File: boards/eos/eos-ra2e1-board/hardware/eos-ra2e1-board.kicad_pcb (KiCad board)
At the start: 2 copper layers, 68.6 x 53.3 mm, 62 parts, among them J1 USB-C, J2 SWD, J3 D8-SCL, J4 D0-D7, J5 POWER, J6 A0-A5, J7 PMOD A, J8 PMOD B, SW1 RESET, SW2 USER, U1 R7FA2E1A92DFM, U2 SP0503BAHTG, U3 CP2102N-A02-GQFN24, U4 TPS7A91, Y1 32.768kHz

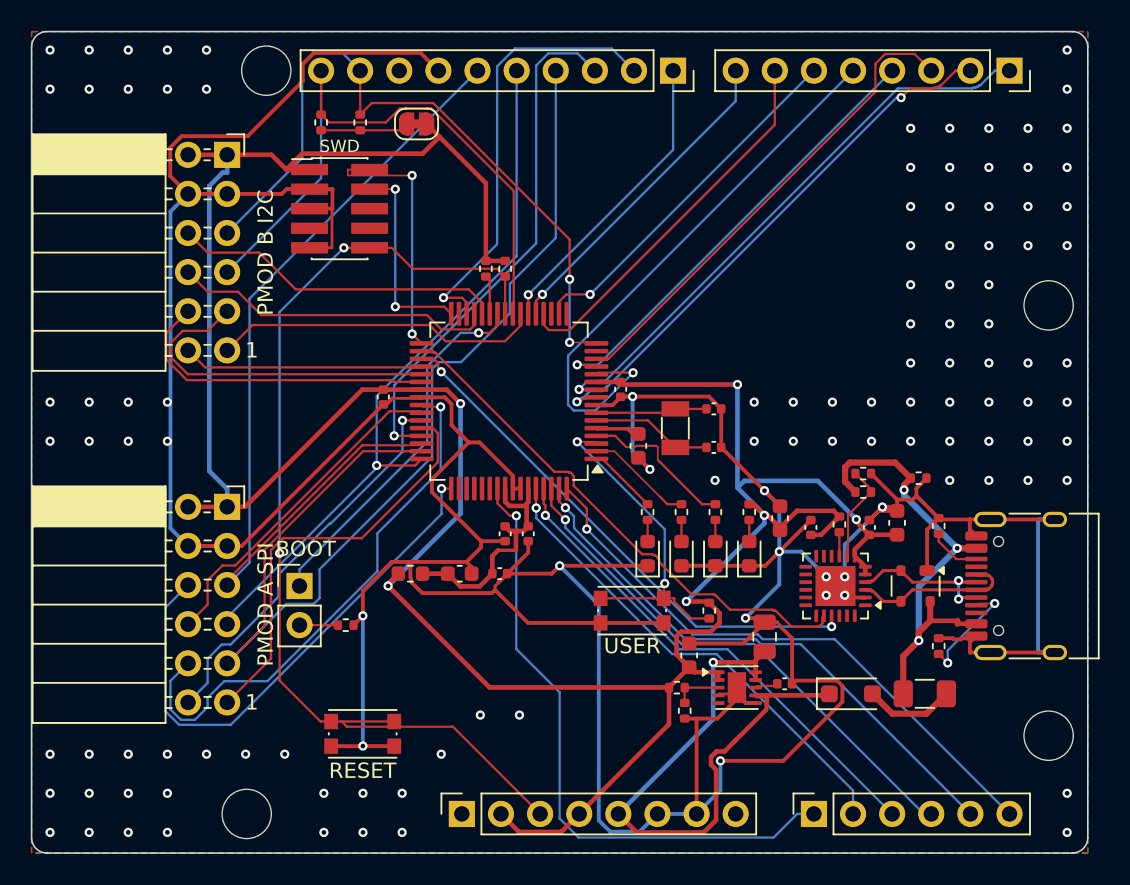
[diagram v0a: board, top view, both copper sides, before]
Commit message: fix(boards): rebuild the ten boards made before the no-via-in-pad rule (#55)
PR #64's generator keeps vias out of surface pads (a chip's exposed pad
aside) and 0.1 mm from their own net's pads. Ten boards on master were built
before that rule and had 34 pads with a via in or beside them. They are
rebuilt with the same generator: ATmega328P, RA2E1, KE16Z, KL25, STM32 64,
ESP32 DevKit, Learn RP2350, LPC55S69, CM4 Base and CM5 Base. Each builds at
ERC 0, DRC errors 0, unconnected 0 and parity 0, with the same parts, values,
nets and positions and the same DRC warnings as before.

Where the router could no longer close a short link without a via in a pad,
or left a ground pad without a good path to a via, the design files use
routing options only: priority routes, fanout_first, ground_vias, and a
bottom-layer router keep-out under KL25's crystal (so RESET_b no longer runs
under it). ViaInPadTest drops BUILT_BEFORE_THE_RULE; it now allows only Learn
RP2350's two Raspberry Pi reference vias, named by position. READMEs, TASKS
and CHANGELOG follow the rebuilt copper. Independent verification: three
rounds; the owner adopted a two-layer pour-island criterion (TASKS.md).

Part of #55.
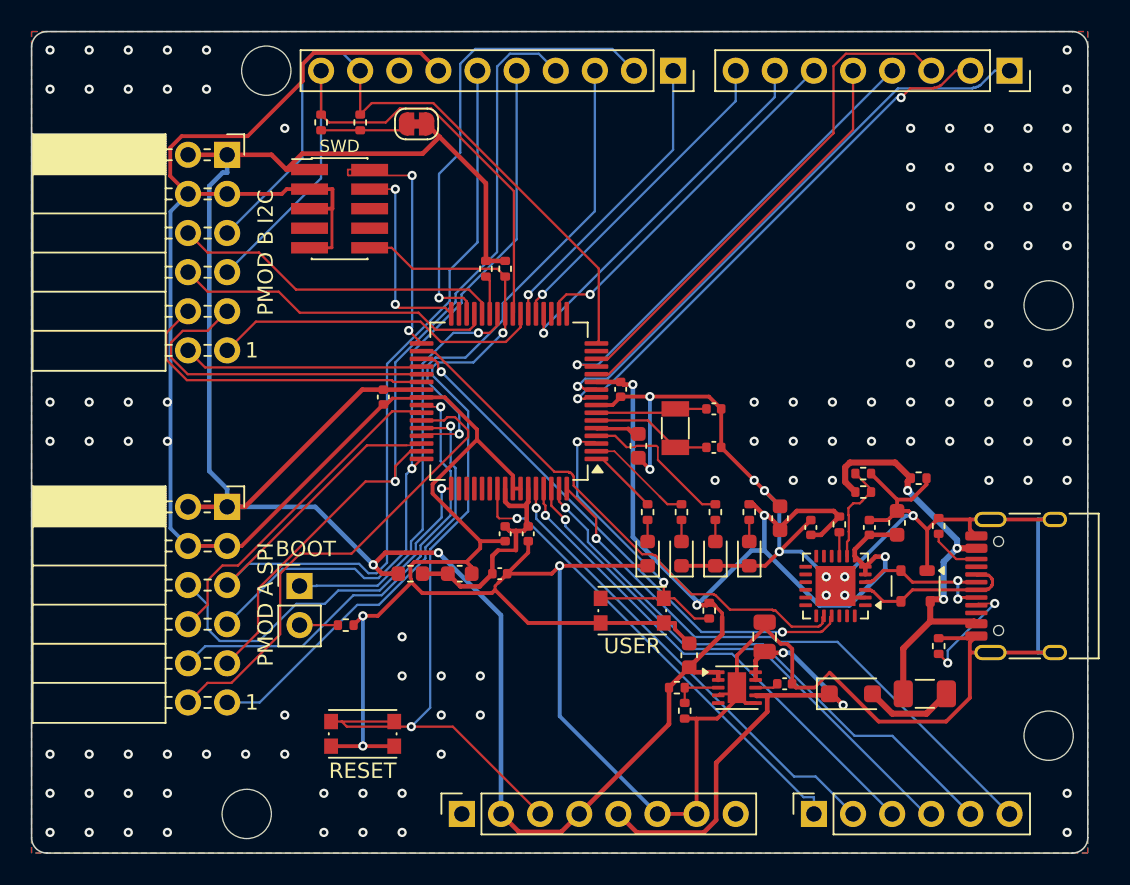
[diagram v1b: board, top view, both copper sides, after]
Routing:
- net /SPI_MOSI: track 70.4 -> 54.9 mm, vias 0 -> 1
- net GND: track 331.0 -> 319.0 mm, vias 114 -> 120
- net /D4: track 37.2 -> 27.1 mm, vias 1 -> 0
- net /A0: track 41.0 -> 31.0 mm
- net /PMODA_CS3: track 35.0 -> 25.1 mm
- net +5V: track 40.0 -> 32.0 mm, vias 1 -> 2
- net /PMODA_INT: track 25.7 -> 31.5 mm, vias 1 -> 0
- net /SPI_SCK: track 56.7 -> 62.3 mm
- net /PMODA_RST: track 35.2 -> 30.1 mm
- net /RES: track 67.4 -> 64.1 mm
- net /MD: track 24.1 -> 27.3 mm
- net /VBUS: track 31.0 -> 28.3 mm
- net /SPI_MISO: track 46.8 -> 49.1 mm
- net +3V3: track 192.7 -> 190.7 mm
- net /D9: track 28.8 -> 30.7 mm
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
